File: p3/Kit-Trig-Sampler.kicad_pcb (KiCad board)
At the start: 2 copper layers, 78 x 109.2 mm, 81 parts, among them J1 START_CV, J10 AUDIO_INR, J11 AUDIO_OUTL, J13 BANK_CV, J14 Eurorack_Power_10pin_Unshroud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, J2 LENGTH_CV, J3 SAMP_CV, J4 PITCH CV, J5 REV_TRIG, J6 PLAY_TRIG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

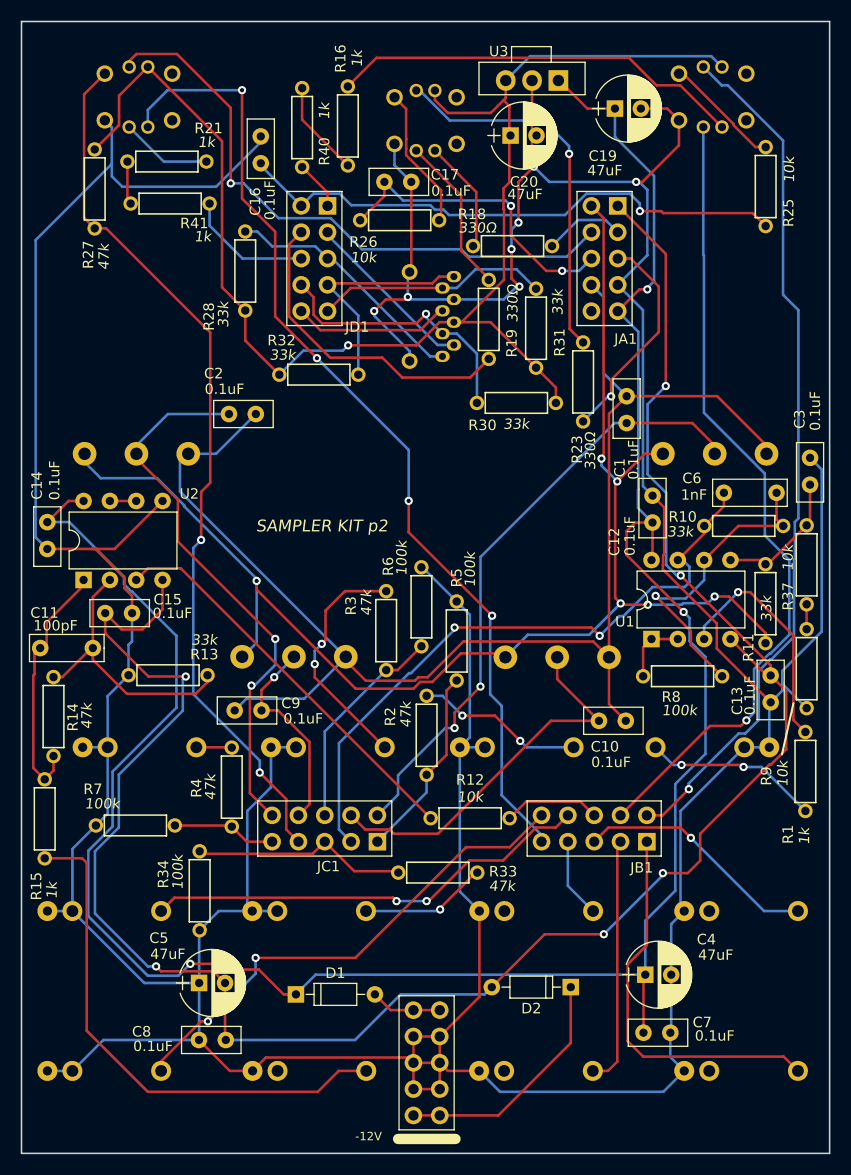
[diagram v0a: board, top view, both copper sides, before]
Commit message: p3: added 47k resistors to Trig Ins
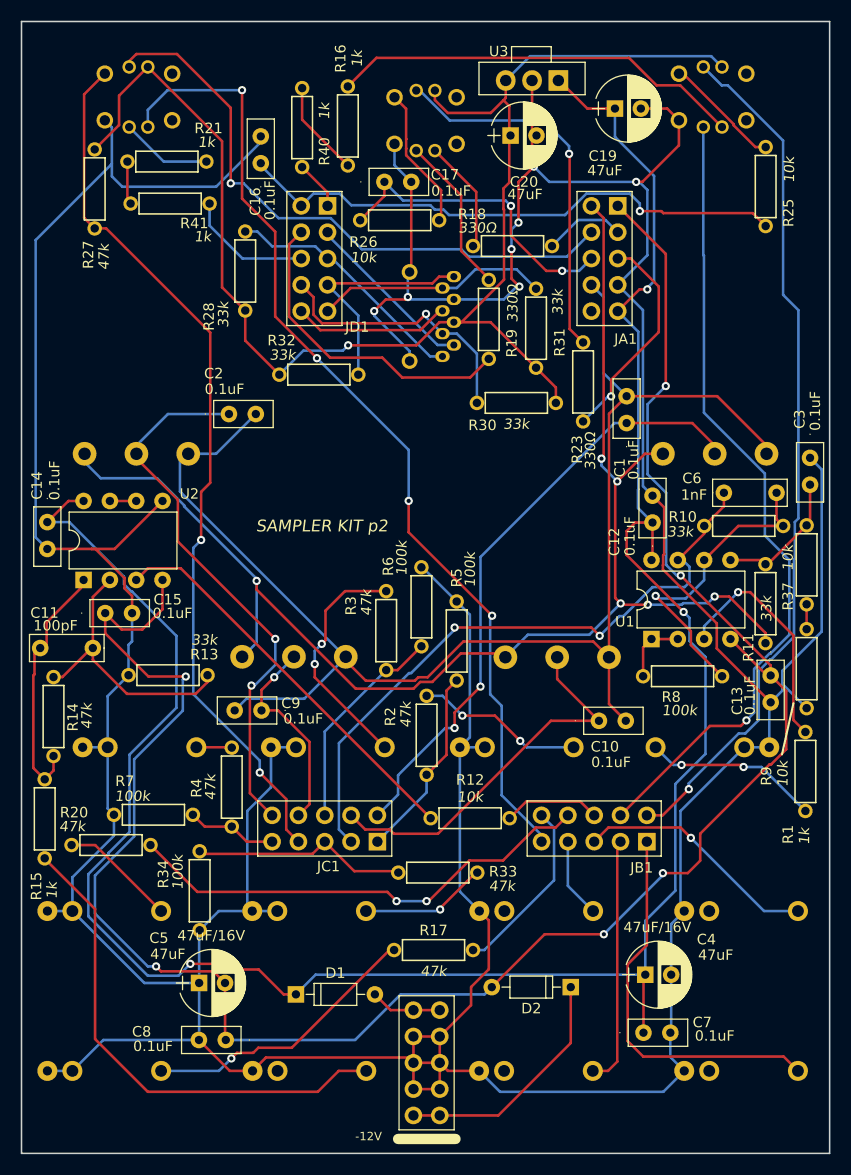
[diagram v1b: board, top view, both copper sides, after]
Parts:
- added R17: 47k_TH0.125, 4ms_Resistor:R_Axial_DIN0207_L6.3mm_D2.5mm_P7.62mm_Horizontal, F.Cu at (51.8, 102.0)
- added R20: 47k_TH0.125, 4ms_Resistor:R_Axial_DIN0207_L6.3mm_D2.5mm_P7.62mm_Horizontal, F.Cu at (20.6, 91.9)
- moved R7 2.02 mm to (24.7, 89.0)
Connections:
- J5 pad 1: /D2 -> Net-(J5-SIG)
- J6 pad 1: /D13 -> Net-(J6-SIG)
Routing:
- net /D2: track 48.4 -> 17.4 mm, vias 2 -> 0
- net Net-(J5-SIG): track 0.00 -> 26.9 mm, vias 0 -> 1
- net Net-(J6-SIG): track 0.00 -> 11.3 mm
- net /D13: track 43.4 -> 45.9 mm
- net Net-(J7-SIG): track 50.7 -> 48.5 mm
- net GND: track 515.1 -> 516.3 mm
- net /A8: track 9.87 -> 8.72 mm

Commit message: p3: generated production files
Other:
- board text added: "SAMPLER KIT p3"
- board text removed: "SAMPLER KIT p2"
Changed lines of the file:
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@@
     (effects (font (size 1 1) (thickness 0.15)) (justify right top mirror))
   )
-  (gr_text "SAMPLER KIT p2" (at 41 61.1) (layer "F.SilkS")
+  (gr_text "SAMPLER KIT p3" (at 41 61.1) (layer "F.SilkS")
     (effects (font (size 1.143 1.143) (thickness 0.1778) italic))
   )

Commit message: Update instructions.pdf, update BOM, export Gerbers
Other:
- board text added: "SAMPLER KIT v1.0"
- board text removed: "SAMPLER KIT p3"
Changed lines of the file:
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@@
     )
     (pad_to_mask_clearance 0)
+    (aux_axis_origin 12.011 121.6438)
     (pcbplotparams
-      (layerselection 0x00010fc_ffffffff)
+      (layerselection 0x00010f0_ffffffff)
       (plot_on_all_layers_selection 0x0000000_00000000)
       (disableapertmacros false)
       (usegerberextensions false)
-      (usegerberattributes true)
+      (usegerberattributes false)
       (usegerberadvancedattributes true)
-      (creategerberjobfile true)
+      (creategerberjobfile false)
       (dashed_line_dash_ratio 12.000000)
       (dashed_line_gap_ratio 3.000000)
@@
       (viasonmask false)
       (mode 1)
-      (useauxorigin false)
+      (useauxorigin true)
       (hpglpennumber 1)
       (hpglpenspeed 20)
@@
       (plotinvisibletext false)
       (sketchpadsonfab false)
-      (subtractmaskfromsilk false)
+      (subtractmaskfromsilk true)
       (outputformat 1)
       (mirror false)
-      (drillshape 1)
+      (drillshape 0)
       (scaleselection 1)
-      (outputdirectory "")
+      (outputdirectory "gbr")
     )
   )
@@
         (effects (font (size 1 1) (thickness 0.15)))
     )
-    (fp_text value "78M33_TH" (at 5.08 2.54) (layer "F.Fab")
+    (fp_text value "78M33_TH" (at 2.465 0.7875) (layer "F.Fab")
         (effects (font (size 1 1) (thickness 0.15)))
     )
@@
     (effects (font (size 1 1) (thickness 0.15)) (justify right top mirror))
   )
-  (gr_text "SAMPLER KIT p3" (at 41 61.1) (layer "F.SilkS")
+  (gr_text "SAMPLER KIT v1.0" (at 41 61.1) (layer "F.SilkS")
     (effects (font (size 1.143 1.143) (thickness 0.1778) italic))
   )
